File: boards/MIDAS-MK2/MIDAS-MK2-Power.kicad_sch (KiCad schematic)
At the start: 31 parts, among them J103 Conn_01x02, J301 TestPoint, U301 TPS2121, U302 TI_TPS566242

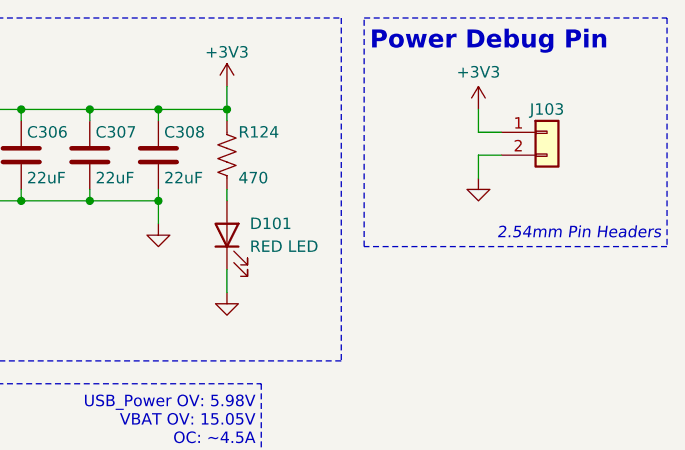
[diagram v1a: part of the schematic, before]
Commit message: swapping pins
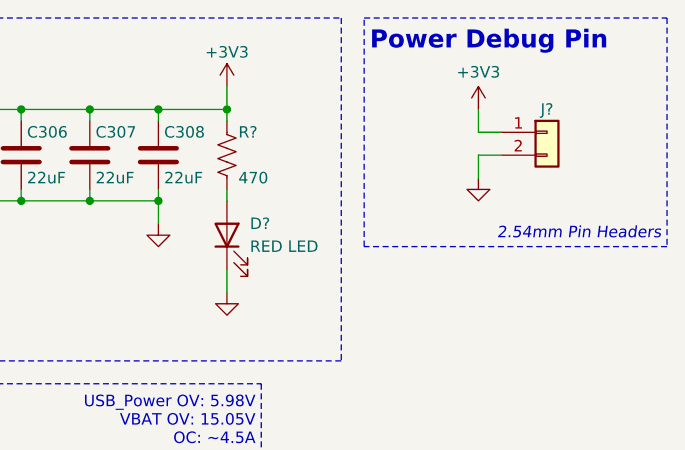
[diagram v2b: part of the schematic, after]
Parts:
- renumbered D101 to D?, J103 to J?, R124 to R?
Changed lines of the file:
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@@
 		(on_board yes)
 		(dnp no)
-		(property "Reference" "D101"
+		(property "Reference" "D?"
 			(at 137.16 38.1 90)
 			(effects
@@
 		(pin "2"
 		)
+		(instances
+			(project "MIDAS-MK2"
+				(path "/6007cf46-4651-4a02-8f98-d5846f3575c7/6a3d8d20-17ea-4f21-96e4-14cd4e641450"
+					(reference "D?")
+					(unit 1)
+				)
+			)
+		)
 	)
 	(symbol
@@
 		(dnp no)
 		(fields_autoplaced yes)
-		(property "Reference" "#PWR0133"
+		(property "Reference" "#PWR?"
 			(at 162.56 29.21 0)
 			(effects
@@
 		(pin "1"
 		)
+		(instances
+			(project "MIDAS-MK2"
+				(path "/6007cf46-4651-4a02-8f98-d5846f3575c7/6a3d8d20-17ea-4f21-96e4-14cd4e641450"
+					(reference "#PWR?")
+					(unit 1)
+				)
+			)
+		)
 	)
 	(symbol
@@
 		(on_board yes)
 		(dnp no)
-		(property "Reference" "R124"
+		(property "Reference" "R?"
 			(at 135.89 27.94 0)
 			(effects
@@
 		)
 		(pin "2"
+		)
+		(instances
+			(project "MIDAS-MK2"
+				(path "/6007cf46-4651-4a02-8f98-d5846f3575c7/6a3d8d20-17ea-4f21-96e4-14cd4e641450"
+					(reference "R?")
+					(unit 1)
+				)
+			)
 		)
 	)
@@
 		(pin "1"
 		)
+		(instances
+			(project "MIDAS-MK2"
+				(path "/6007cf46-4651-4a02-8f98-d5846f3575c7/6a3d8d20-17ea-4f21-96e4-14cd4e641450"
+					(reference "#PWR?")
+					(unit 1)
+				)
+			)
+		)
 	)
 	(symbol
@@
 		(on_board yes)
 		(dnp no)
-		(property "Reference" "J103"
+		(property "Reference" "J?"
 			(at 170.18 25.4 0)
 			(effects
@@
 		)
 		(pin "2"
+		)
+		(instances
+			(project "MIDAS-MK2"
+				(path "/6007cf46-4651-4a02-8f98-d5846f3575c7/6a3d8d20-17ea-4f21-96e4-14cd4e641450"
+					(reference "J?")
+					(unit 1)
+				)
+			)
 		)
 	)
@@
 		(dnp no)
 		(fields_autoplaced yes)
-		(property "Reference" "#PWR0134"
+		(property "Reference" "#PWR?"
 			(at 162.56 39.37 0)
 			(effects
@@
 		(pin "1"
 		)
-	)
+		(instances
+			(project "MIDAS-MK2"
+				(path "/6007cf46-4651-4a02-8f98-d5846f3575c7/6a3d8d20-17ea-4f21-96e4-14cd4e641450"
+					(reference "#PWR?")
+					(unit 1)
+				)
+			)
+		)
+	)

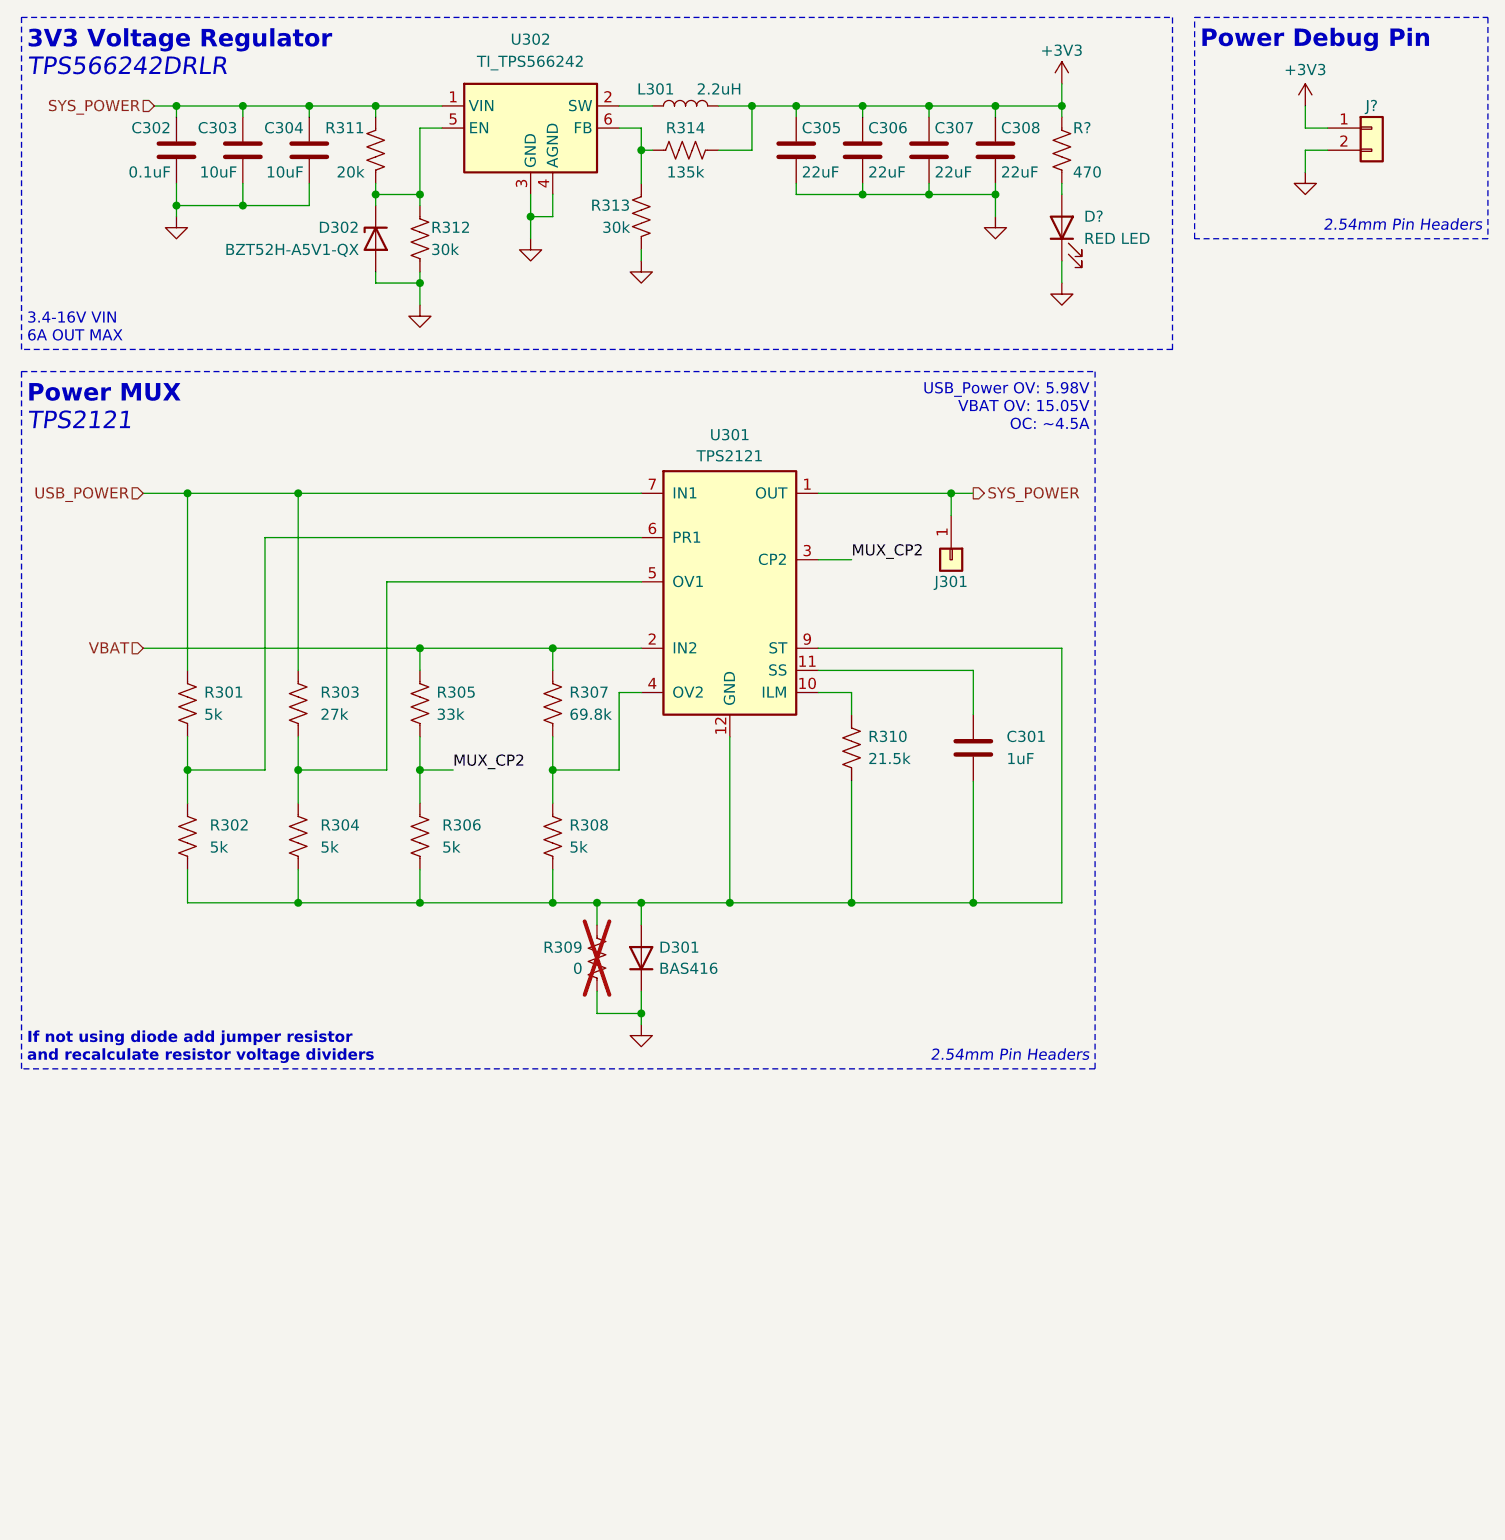
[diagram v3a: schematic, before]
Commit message: Added TVS Diodes to Power
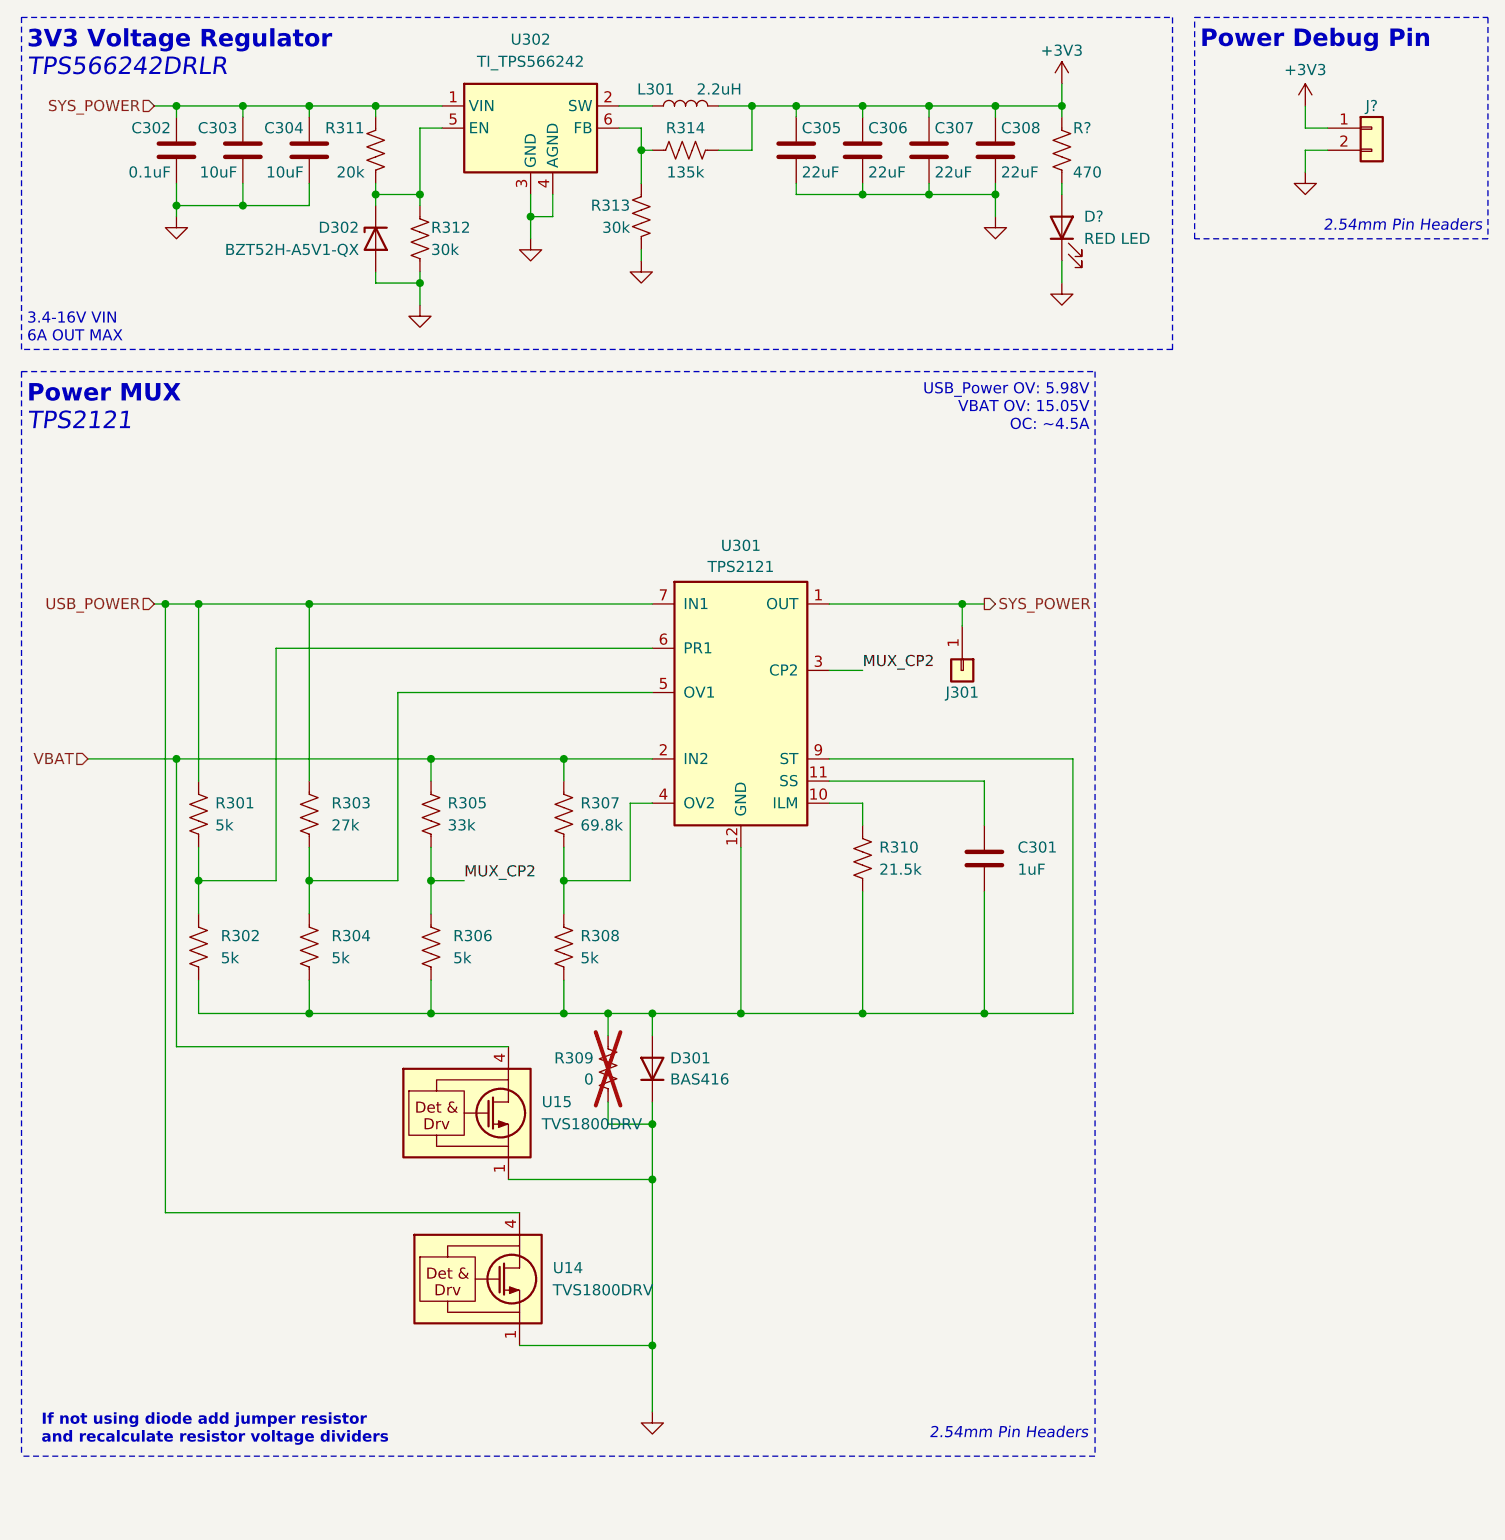
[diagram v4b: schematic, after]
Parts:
- added U14, U15: TVS1800DRV, Package_SON:WSON-6-1EP_2x2mm_P0.65mm_EP1x1.6mm, symbol Power_Protection:TVS1800DRV
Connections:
- net GND: now also U14.1 (GND), U14.2 (GND), U14.3 (GND), U14.7 (GND), U15.1 (GND), U15.2 (GND), U15.3 (GND), U15.7 (GND)
- net USB_POWER: now also U14.4 (IN), U14.5 (IN), U14.6 (IN)
- net VBAT: now also U15.4 (IN), U15.5 (IN), U15.6 (IN)
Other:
- moved on the sheet: C301, D301, J301, R301, R302, R303, R304, R305, R306, R307, R308, R309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

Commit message: Fixing formatting for TVS Diodes in Schematic (making it more pretty)
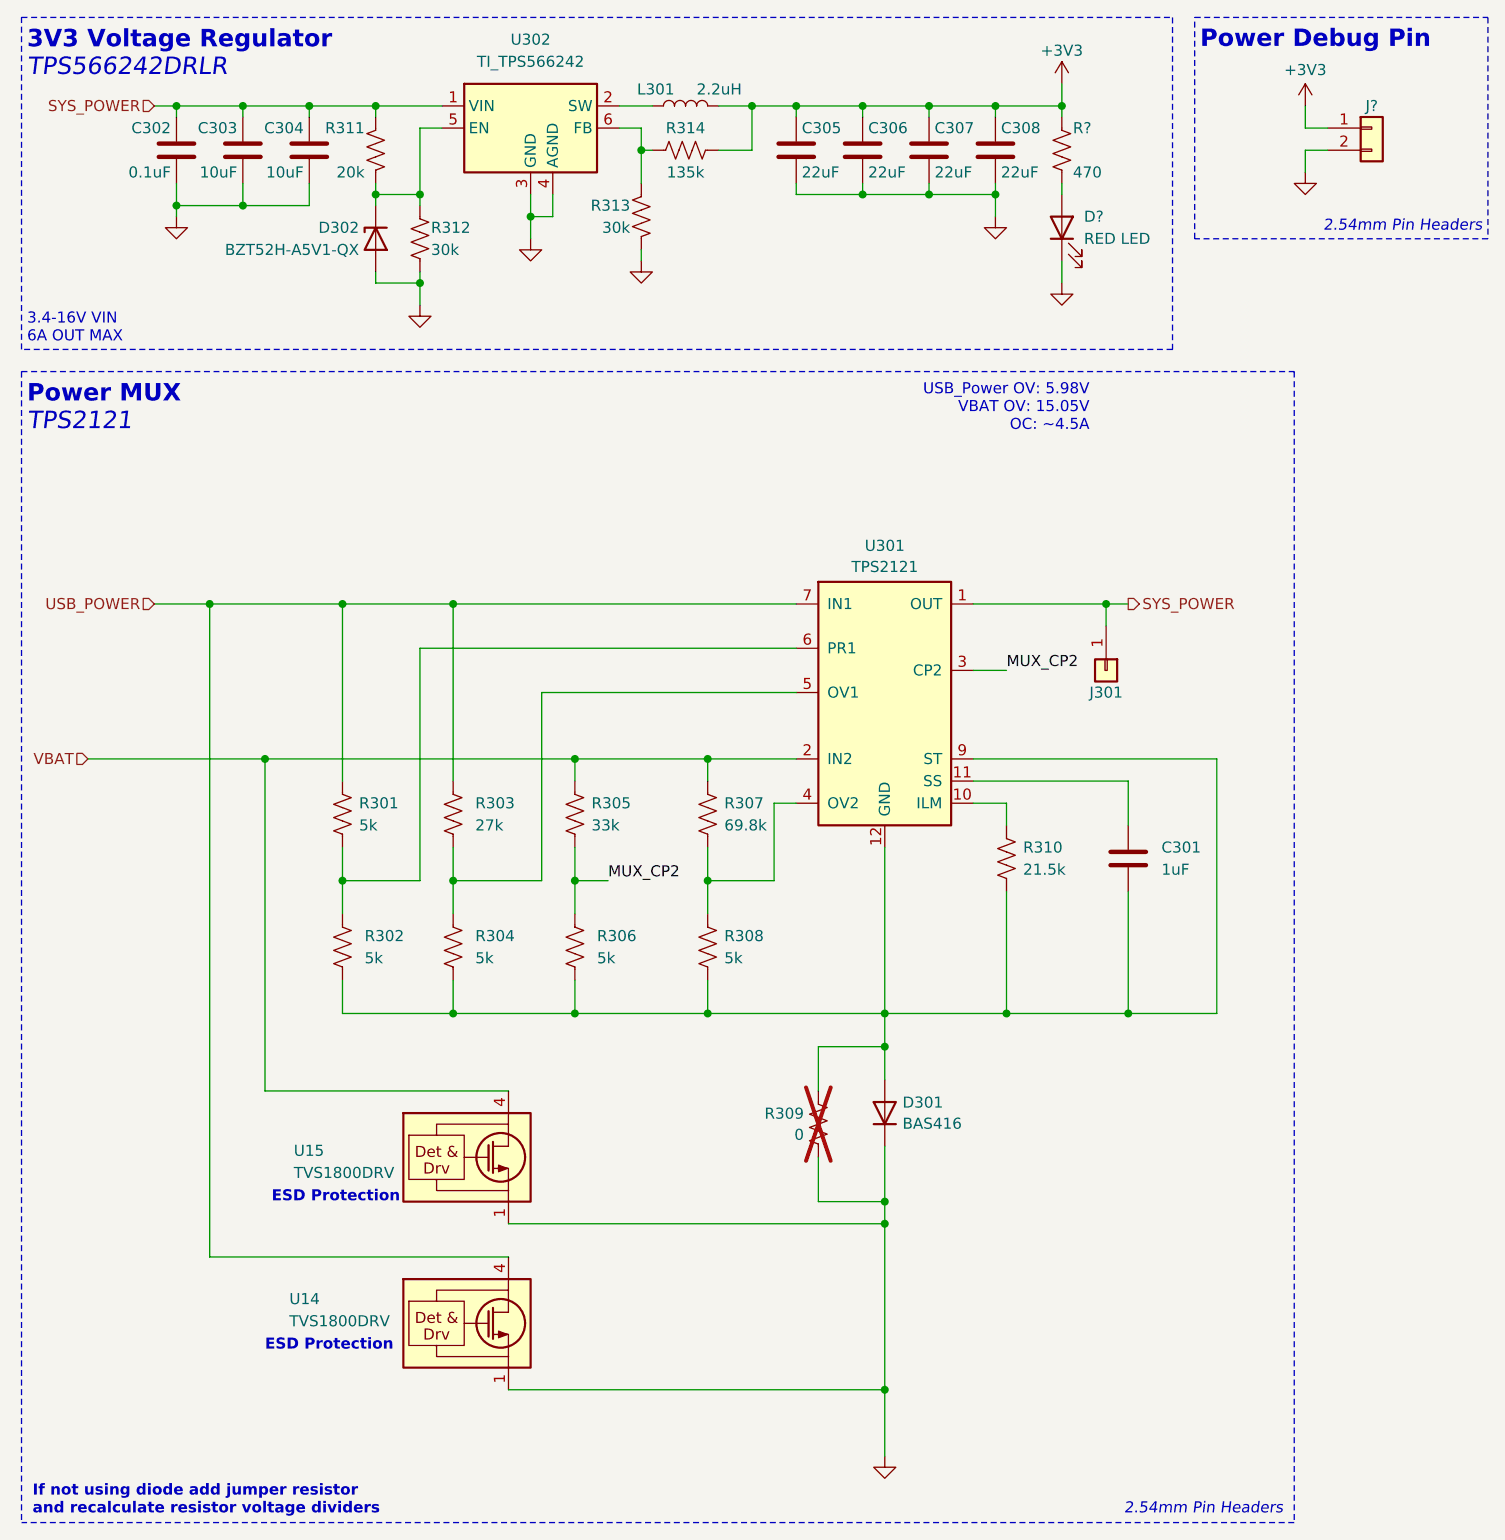
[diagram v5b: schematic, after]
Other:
- note added: "ESD Protection"
- moved on the sheet: C301, D301, J301, R301, R302, R303, R304, R305, R306, R307, R308, R309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

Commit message: general changes, reorganization, etc.
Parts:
- removed U14, U15: TVS1800DRV, Package_SON:WSON-6-1EP_2x2mm_P0.65mm_EP1x1.6mm, symbol Power_Protection:TVS1800DRV
- R301, R302, R304, R306, R308: footprint Resistor_SMD:R_0603_1608Metric -> Capacitor_SMD:C_0603_1608Metric
- U301: footprint Package_VQFN:VQFN-HR-RUX0012A -> Package_DFN_QFN:Texas_VQFN-HR-12_2x2.5mm_P0.5mm
- gave numbers to parts that had none: 3
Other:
- note removed: "ESD Protection"
- moved on the sheet: C301, D301, J301, R301, R302, R303, R304, R305, R306, R307, R308, R309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

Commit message: fixed resistor footprints
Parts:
- R301, R302, R304, R306, R308: footprint Capacitor_SMD:C_0603_1608Metric -> Resistor_SMD:R_0603_1608Metric
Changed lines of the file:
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@@
 			)
 		)
-		(property "Footprint" "Capacitor_SMD:C_0603_1608Metric"
+		(property "Footprint" "Resistor_SMD:R_0603_1608Metric"
 			(at 48.006 109.474 90)
 			(effects
@@
 			)
 		)
-		(property "Footprint" "Capacitor_SMD:C_0603_1608Metric"
+		(property "Footprint" "Resistor_SMD:R_0603_1608Metric"
 			(at 35.306 109.474 90)
 			(effects
@@
 			)
 		)
-		(property "Footprint" "Capacitor_SMD:C_0603_1608Metric"
+		(property "Footprint" "Resistor_SMD:R_0603_1608Metric"
 			(at 35.306 94.234 90)
 			(effects
@@
 			)
 		)
-		(property "Footprint" "Capacitor_SMD:C_0603_1608Metric"
+		(property "Footprint" "Resistor_SMD:R_0603_1608Metric"
 			(at 77.216 109.474 90)
 			(effects
@@
 			)
 		)
-		(property "Footprint" "Capacitor_SMD:C_0603_1608Metric"
+		(property "Footprint" "Resistor_SMD:R_0603_1608Metric"
 			(at 61.976 109.474 90)
 			(effects

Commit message: schematics done
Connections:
- net SYS_POWER: no longer C302.1, C303.1, C304.1, R311.1, U302.1 (VIN)
- new net VREG_IN: C302.1, C303.1, C304.1, R311.1, U302.1 (VIN)
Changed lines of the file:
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@@
 	(title_block
 		(title "MIDAS Power Circuitry MK2")
-		(date "2024-09-03")
+		(date "2024-11-04")
 		(rev "A")
 		(company "Illinois Space Society")
@@
 		)
 	)
-	(hierarchical_label "SYS_POWER"
+	(hierarchical_label "VREG_IN"
 		(shape input)
 		(at 30.48 25.4 180)
